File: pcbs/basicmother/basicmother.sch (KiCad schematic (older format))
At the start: 9 parts, among them P1 ZIGBIT_DIP, P2 Eyes-comm, P3 L-MOTOR, P4 R-MOTOR, U1 ZIGBIT_DUAL_DIP, U2 MBED, U3 bluetooth-mod

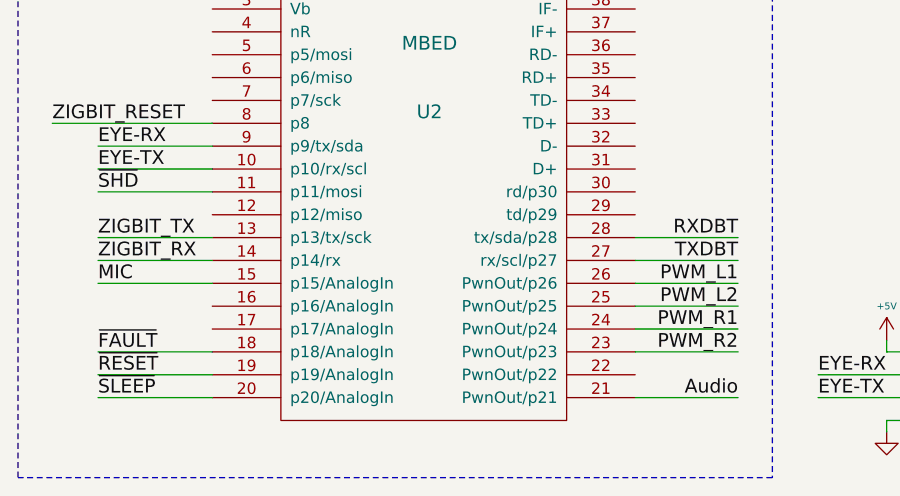
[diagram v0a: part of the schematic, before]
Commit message: primera version del pcb de la placa principal, falta verificar footprints
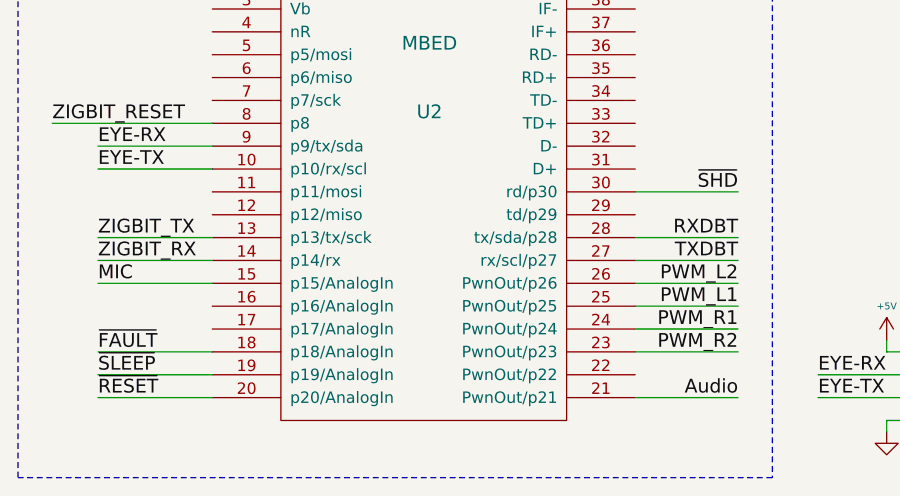
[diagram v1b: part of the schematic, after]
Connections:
- net PWM_L1: now also U2.25 (PwnOut/p25); no longer U2.26 (PwnOut/p26)
- net PWM_L2: now also U2.26 (PwnOut/p26); no longer U2.25 (PwnOut/p25)
- net ~RESET: now also U2.20 (p20/AnalogIn); no longer U2.19 (p19/AnalogIn)
- net ~SHD: now also U2.30 (rd/p30); no longer U2.11 (p11/mosi)
- net ~SLEEP: now also U2.19 (p19/AnalogIn); no longer U2.20 (p20/AnalogIn)
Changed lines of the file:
@@
 Wire Wire Line
 	3300 7100 3750 7100
+Text Label 3750 6900 2    60   ~ 0
+PWM_L1
 Text Label 3750 6800 2    60   ~ 0
-PWM_L1
-Text Label 3750 6900 2    60   ~ 0
 PWM_L2
 Text Label 3750 7000 2    60   ~ 0
@@
 Text Label 5200 4600 0    60   ~ 0
 ~SHD
-Text Label 950  6400 0    60   ~ 0
+Text Label 3750 6400 2    60   ~ 0
 ~SHD
-Wire Wire Line
-	950  6400 1450 6400
 Wire Wire Line
 	1450 5500 850  5500
@@
 	1    0    0    -1
 $EndComp
-Text Label 950  7200 0    60   ~ 0
+Text Label 950  7300 0    60   ~ 0
 ~RESET
 Text Label 950  7100 0    60   ~ 0
 ~FAULT
-Text Label 950  7300 0    60   ~ 0
+Text Label 950  7200 0    60   ~ 0
 ~SLEEP
 Wire Wire Line
@@
 Wire Wire Line
 	4400 7100 4500 7100
+Wire Wire Line
+	3750 6400 3300 6400
 $EndSCHEMATC

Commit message: cambios hechos en las placas
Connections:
- net GND: now also P1.10, P1.11, P1.12, P1.13, P1.14, P1.15
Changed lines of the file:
@@
 DIPSW_8
-Wire Wire Line
-	2450 1950 2450 1250
 Wire Wire Line
 	2450 1250 2700 1250
@@
 Wire Wire Line
 	3750 6400 3300 6400
+Wire Wire Line
+	2550 1250 2550 1950
+Wire Wire Line
+	2550 1950 2450 1950
+Connection ~ 2550 1250
+Wire Wire Line
+	2450 1850 2550 1850
+Connection ~ 2550 1850
+Wire Wire Line
+	2450 1750 2550 1750
+Connection ~ 2550 1750
+Wire Wire Line
+	2450 1650 2550 1650
+Connection ~ 2550 1650
+Wire Wire Line
+	2450 1550 2550 1550
+Connection ~ 2550 1550
+Wire Wire Line
+	2450 1450 2550 1450
+Connection ~ 2550 1450
+Wire Wire Line
+	2450 1350 2550 1350
+Connection ~ 2550 1350
 $EndSCHEMATC
